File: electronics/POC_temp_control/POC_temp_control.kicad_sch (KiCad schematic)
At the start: 206 parts, among them J1 Conn_01x02, J2 Conn_01x07, J3 Conn_01x05, J4 Conn_01x06, J5 Conn_01x04, J6 Conn_01x06, Q1 PXT8050, Q10 BC847A, Q11 BC858B, Q12 BC847A, Q2 PXT8050, Q3 PXT8550, Q4 Q_PMOS_DUAL, Q5 Q_PMOS_DUAL, Q6 BC858B, Q7 BC858B, Q8 BC847A, Q9 BC847A, T1 10P_1P_2S, U1 SY8120, U2 MCP1702T-3302, U4 LM358, U5 OP07, U6 OP07, U7 OP07, U8 74XX4051, U9 74XX4051

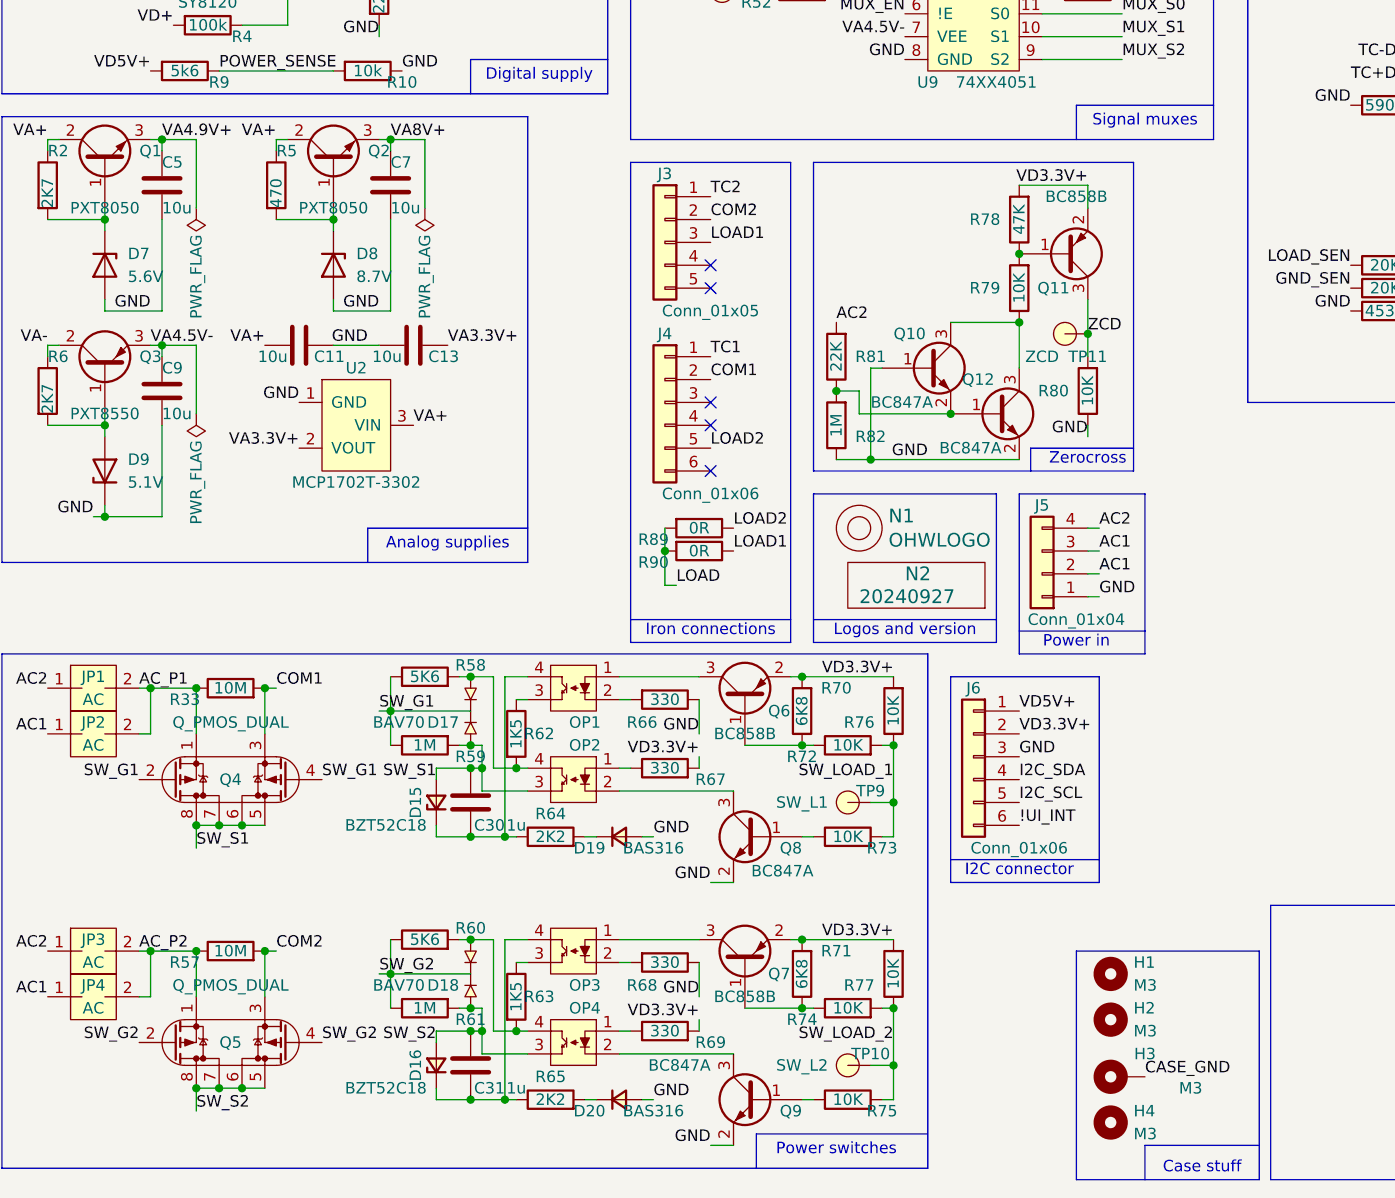
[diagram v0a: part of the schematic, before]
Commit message: updated silk placement
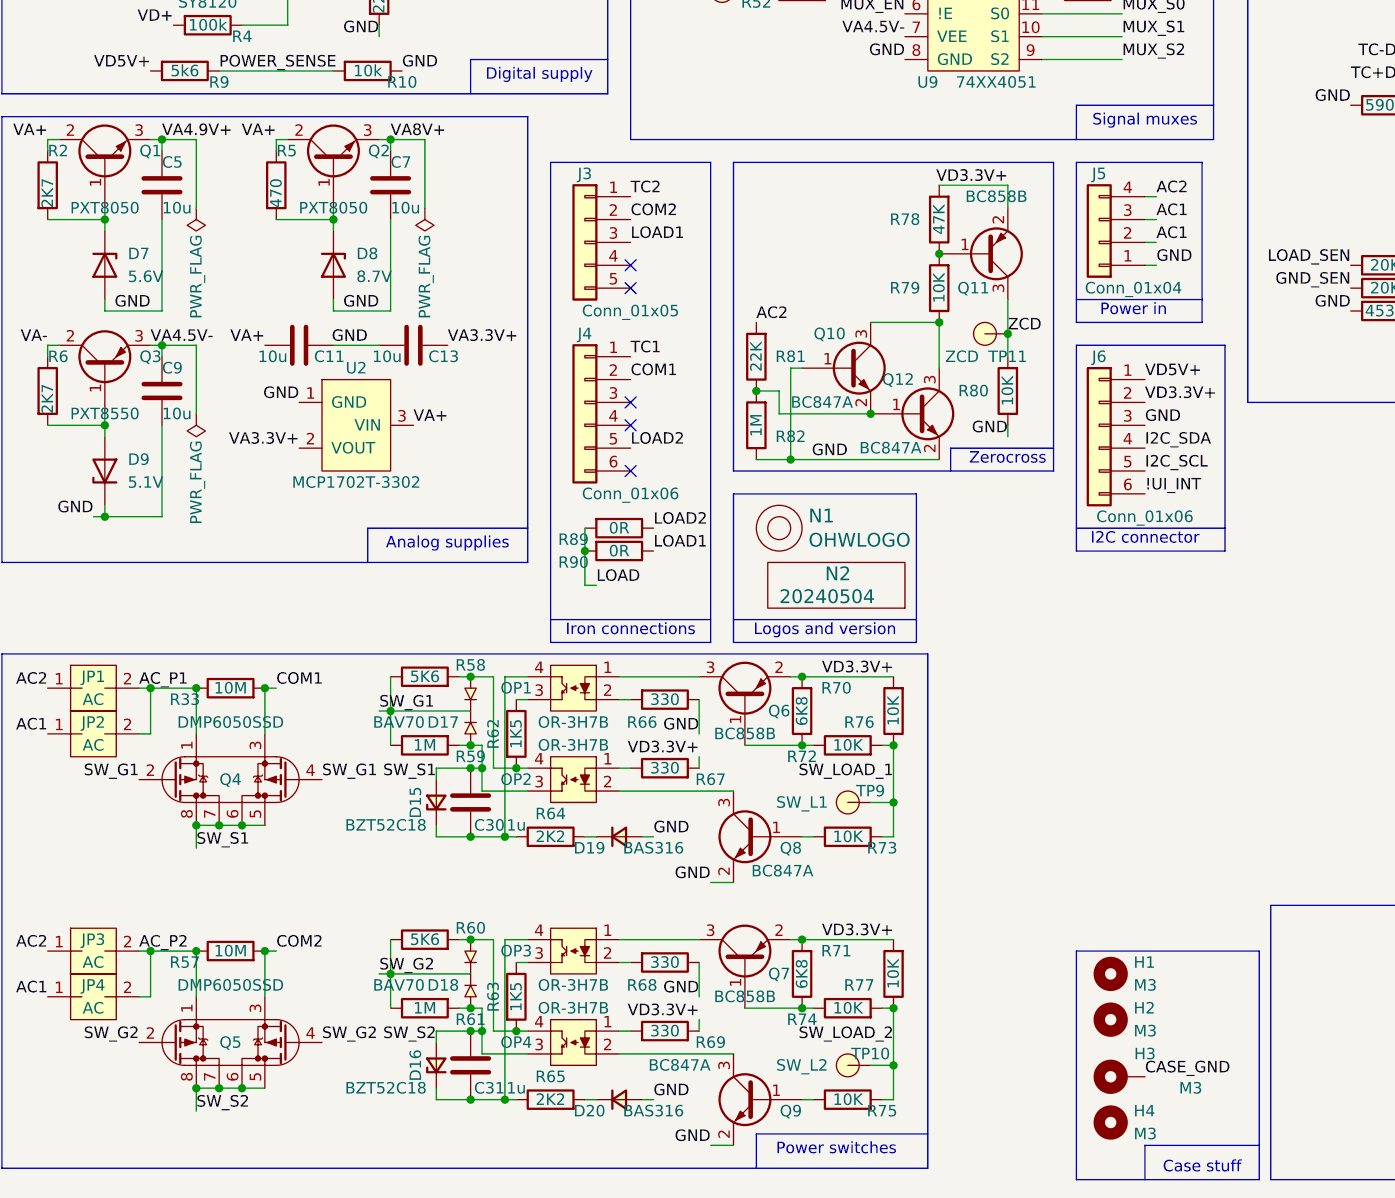
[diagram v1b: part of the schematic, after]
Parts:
- N2: value 20240927 -> 20240504
- OP1, OP2, OP3, OP4: value ~ -> OR-3H7B
- Q4, Q5: value Q_PMOS_DUAL -> DMP6050SSD
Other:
- moved on the sheet: J3, J4, J5, J6, N1, N2, Q10, Q11, Q12, R78, R79, R80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

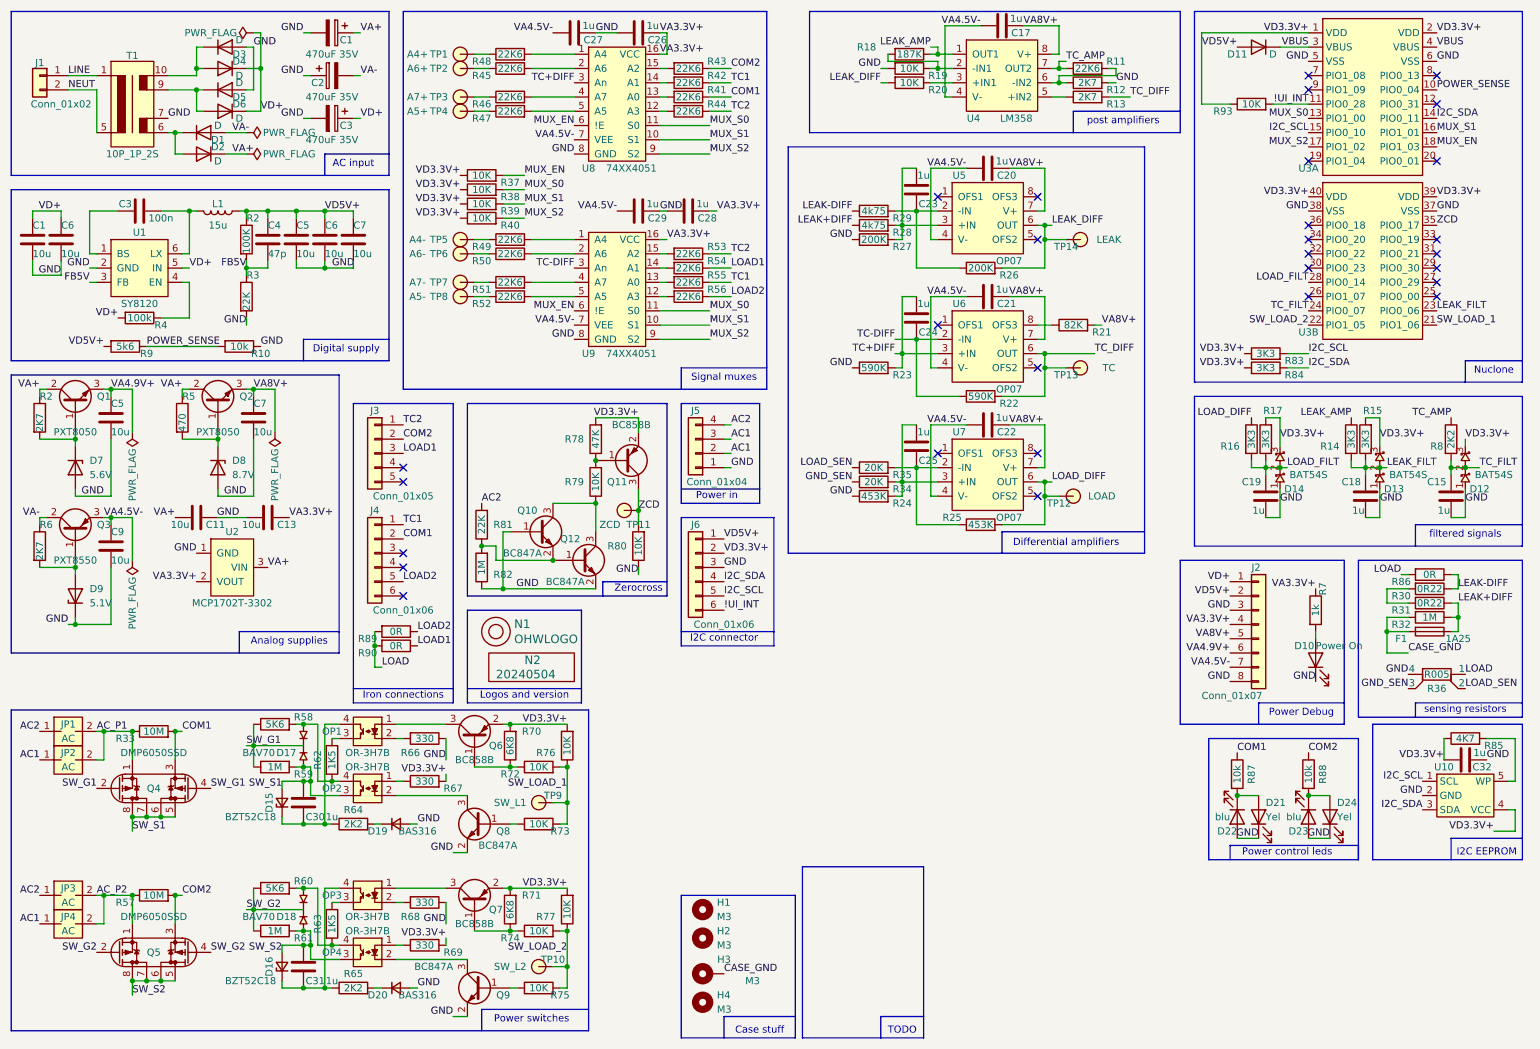
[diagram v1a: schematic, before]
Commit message: added values to all components
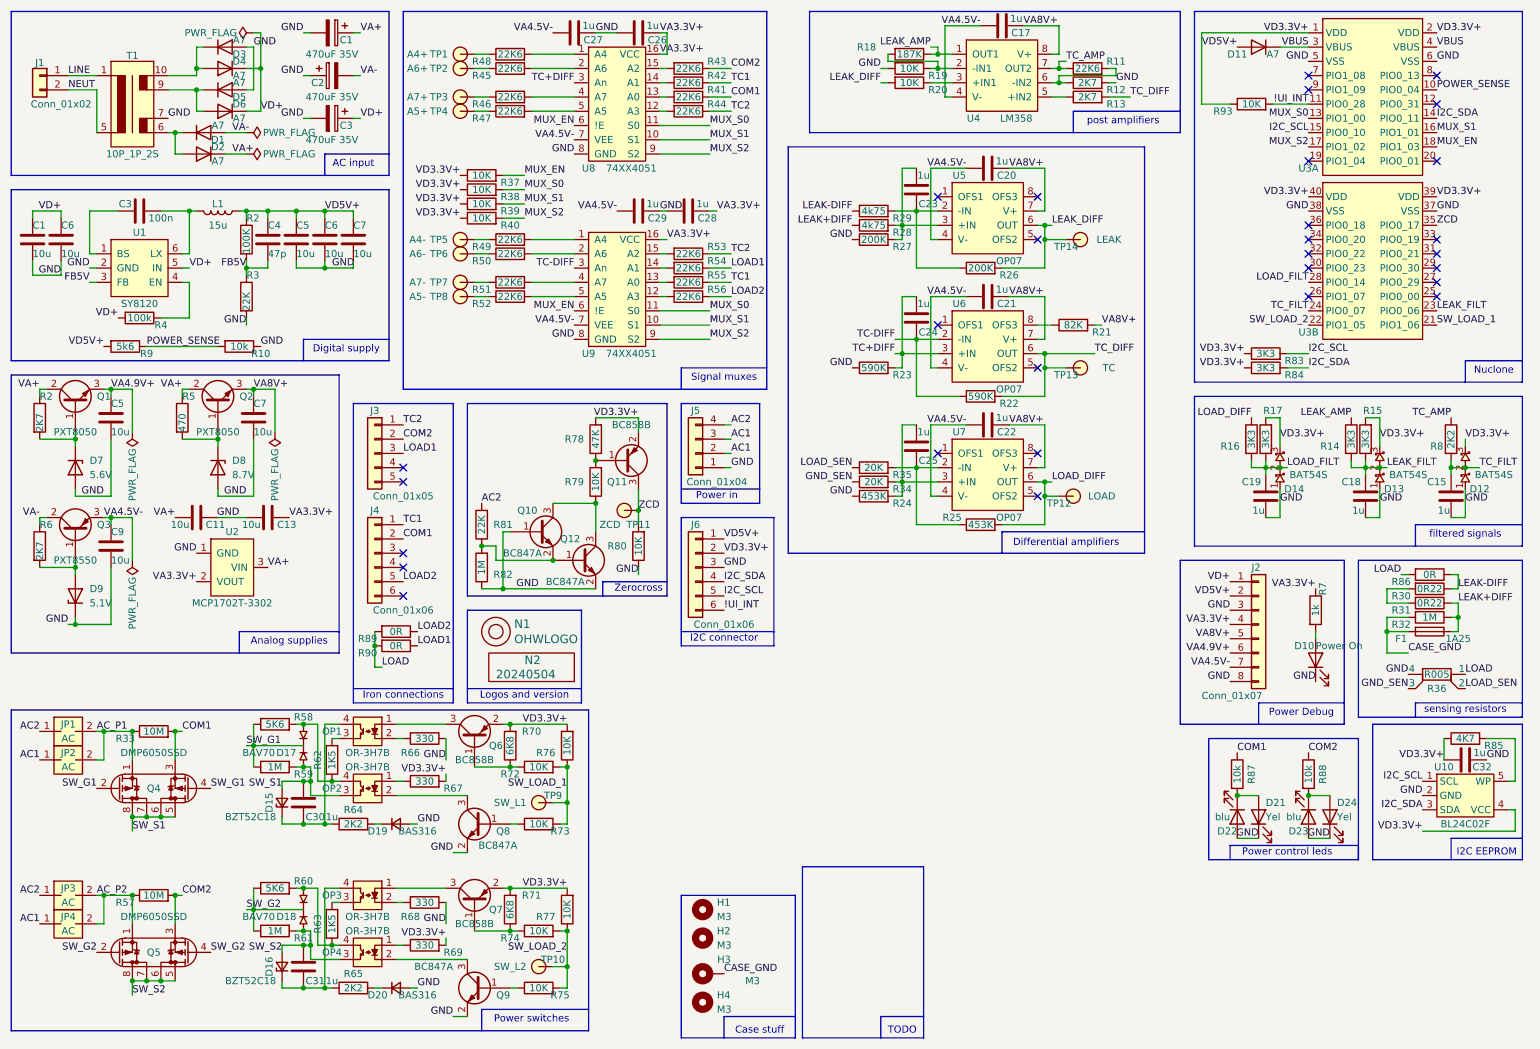
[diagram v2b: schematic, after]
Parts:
- D1, D11, D2, D3, D4, D5, D6: value D -> A7
- U10: value ~ -> BL24C02F
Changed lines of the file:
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@@
 	(wire
 		(pts
-			(xy 278.13 160.02) (xy 281.94 160.02)
+			(xy 265.43 160.02) (xy 281.94 160.02)
 		)
 		(stroke
@@
 	)
 	(label "VD3.3V+"
-		(at 278.13 160.02 180)
+		(at 265.43 160.02 180)
 		(effects
 			(font
@@
 			)
 		)
-		(property "Value" "D"
+		(property "Value" "A7"
 			(at 54.61 19.05 0)
 			(effects
@@
 			)
 		)
-		(property "Value" "D"
+		(property "Value" "A7"
 			(at 50.8 40.64 0)
 			(effects
@@
 			)
 		)
-		(property "Value" "D"
+		(property "Value" "A7"
 			(at 54.61 33.02 0)
 			(effects
@@
 			)
 		)
-		(property "Value" "D"
+		(property "Value" "A7"
 			(at 54.61 25.4 0)
 			(effects
@@
 			)
 		)
-		(property "Value" "D"
+		(property "Value" "A7"
 			(at 238.76 21.59 0)
 			(effects
@@
 			)
 		)
-		(property "Value" "D"
+		(property "Value" "A7"
 			(at 50.8 34.29 0)
 			(effects
@@
 			)
 		)
-		(property "Value" "~"
-			(at 273.05 148.59 0)
+		(property "Value" "BL24C02F"
+			(at 273.05 158.75 0)
 			(effects
 				(font
@@
 			)
 		)
-		(property "Value" "D"
+		(property "Value" "A7"
 			(at 54.61 26.67 0)
 			(effects

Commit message: changed/updated component values
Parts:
- R2: value 100K -> 110K
- R3: value 22K -> 15K
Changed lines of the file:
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@@
 			)
 		)
-		(property "Value" "100K"
+		(property "Value" "110K"
 			(at 55.88 57.15 90)
 			(effects
@@
 			)
 		)
-		(property "Value" "22K"
+		(property "Value" "15K"
 			(at 55.88 67.31 90)
 			(effects
